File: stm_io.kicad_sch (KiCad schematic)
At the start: 0 parts

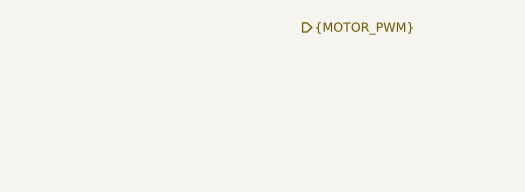
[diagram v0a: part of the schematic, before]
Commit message: schematic: continue project architecture
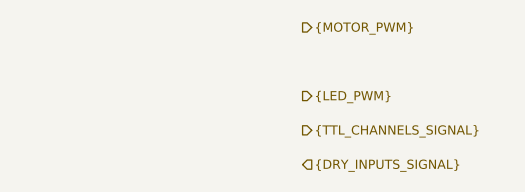
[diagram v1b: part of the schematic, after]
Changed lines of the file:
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@@
 	(generator_version "9.0")
 	(paper "A4")
+	(hierarchical_label "{DRY_INPUTS_SIGNAL}"
+		(shape input)
+		(at 181.61 66.04 0)
+		(effects
+			(font
+				(size 1.016 1.016)
+			)
+			(justify left)
+		)
+	)
 	(hierarchical_label "{MOTOR_PWM}"
 		(shape output)
@@
 		)
 	)
+	(hierarchical_label "{LED_PWM}"
+		(shape output)
+		(at 181.61 58.42 0)
+		(effects
+			(font
+				(size 1.016 1.016)
+			)
+			(justify left)
+		)
+	)
 	(hierarchical_label "H_BEAT"
 		(shape input)
@@
 		)
 	)
+	(hierarchical_label "{TTL_CHANNELS_SIGNAL}"
+		(shape output)
+		(at 181.61 62.23 0)
+		(effects
+			(font
+				(size 1.016 1.016)
+			)
+			(justify left)
+		)
+	)

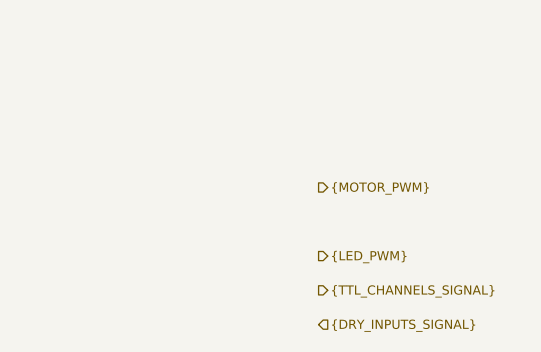
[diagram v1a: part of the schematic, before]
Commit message: schematic: add project structure wiring
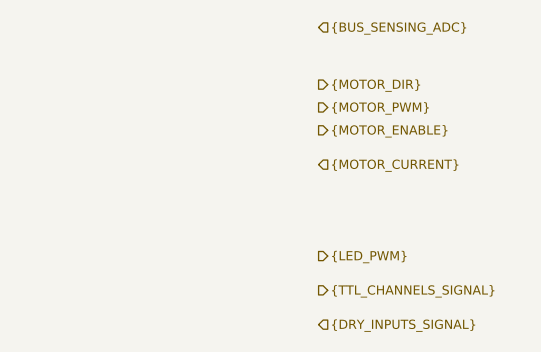
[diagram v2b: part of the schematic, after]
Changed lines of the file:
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@@
 		)
 	)
-	(hierarchical_label "{MOTOR_PWM}"
+	(hierarchical_label "{MOTOR_ENABLE}"
 		(shape output)
-		(at 181.61 50.8 0)
+		(at 181.61 44.45 0)
+		(effects
+			(font
+				(size 1.016 1.016)
+			)
+			(justify left)
+		)
+	)
+	(hierarchical_label "{MOTOR_DIR}"
+		(shape output)
+		(at 181.61 39.37 0)
 		(effects
 			(font
@@
 			)
 			(justify right)
+		)
+	)
+	(hierarchical_label "{BUS_SENSING_ADC}"
+		(shape input)
+		(at 181.61 33.02 0)
+		(effects
+			(font
+				(size 1.016 1.016)
+			)
+			(justify left)
 		)
 	)
@@
 		)
 	)
+	(hierarchical_label "{MOTOR_PWM}"
+		(shape output)
+		(at 181.61 41.91 0)
+		(effects
+			(font
+				(size 1.016 1.016)
+			)
+			(justify left)
+		)
+	)
 	(hierarchical_label "{UART}"
 		(shape bidirectional)
@@
 		)
 	)
+	(hierarchical_label "{MOTOR_CURRENT}"
+		(shape input)
+		(at 181.61 48.26 0)
+		(effects
+			(font
+				(size 1.016 1.016)
+			)
+			(justify left)
+		)
+	)

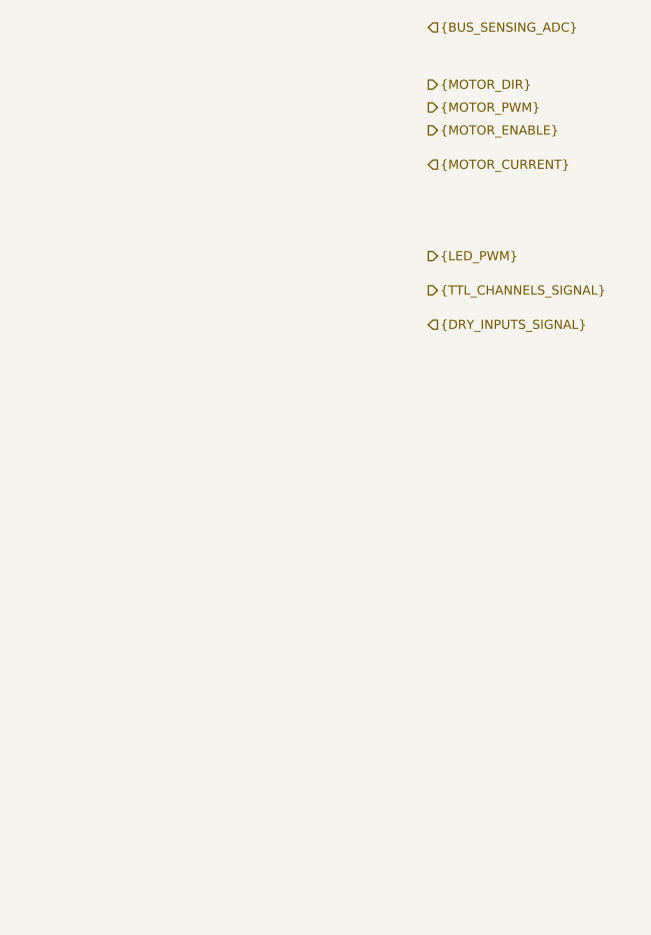
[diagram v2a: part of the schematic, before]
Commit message: Add power stages
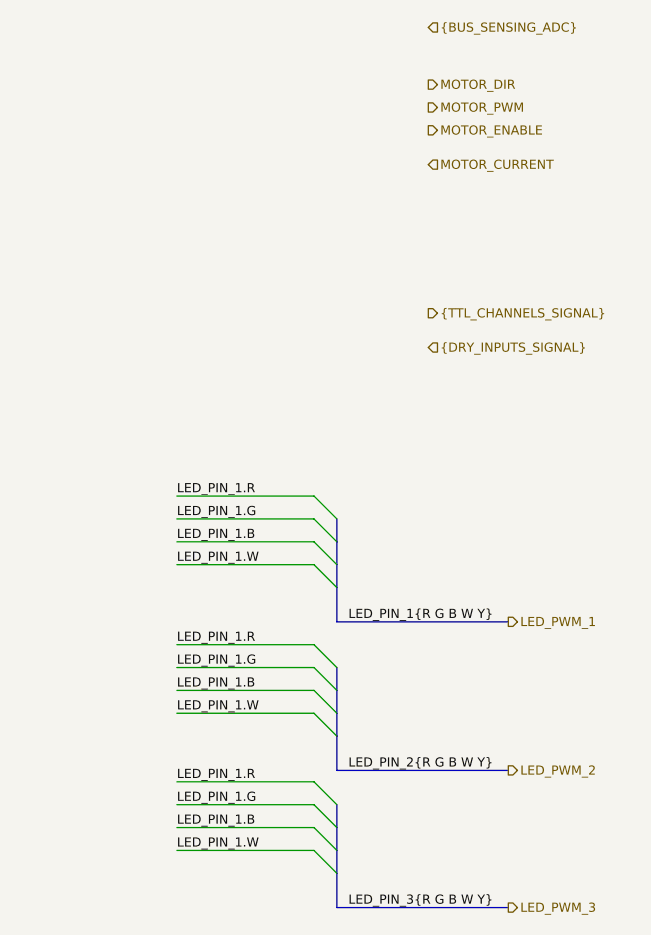
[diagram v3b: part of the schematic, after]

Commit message: Add power supplies
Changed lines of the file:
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@@
+		)
+	)
+	(hierarchical_label "LED_CURRENT"
+		(shape input)
+		(at 191.77 148.59 180)
+		(effects
+			(font
+				(size 1.016 1.016)
+			)
+			(justify right)
 		)
 	)
@@
 			)
 			(justify left)
+		)
+	)
+	(hierarchical_label "~{FAULT}"
+		(shape input)
+		(at 191.77 142.24 180)
+		(effects
+			(font
+				(size 1.016 1.016)
+			)
+			(justify right)
 		)
 	)
@@
 		)
 	)
-	(hierarchical_label "{BUS_SENSING_ADC}"
+	(hierarchical_label "BUS_SENSING_ADC"
 		(shape input)
 		(at 181.61 33.02 0)
@@
 			)
 			(justify left)
+		)
+	)
+	(hierarchical_label "~{FAULT_RESET}"
+		(shape output)
+		(at 191.77 144.78 180)
+		(effects
+			(font
+				(size 1.016 1.016)
+			)
+			(justify right)
 		)
 	)
@@
 		)
 	)
+	(hierarchical_label "CURRENT_LIMIT_SET"
+		(shape output)
+		(at 191.77 139.7 180)
+		(effects
+			(font
+				(size 1.016 1.016)
+			)
+			(justify right)
+		)
+	)

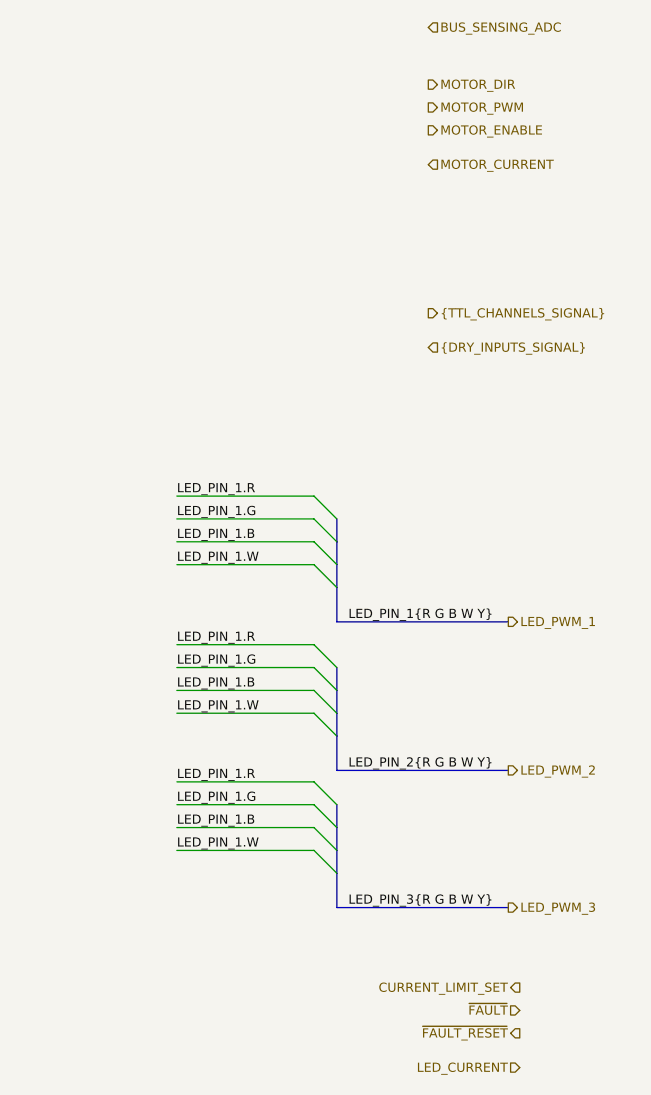
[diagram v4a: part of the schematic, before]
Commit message: Remove STM
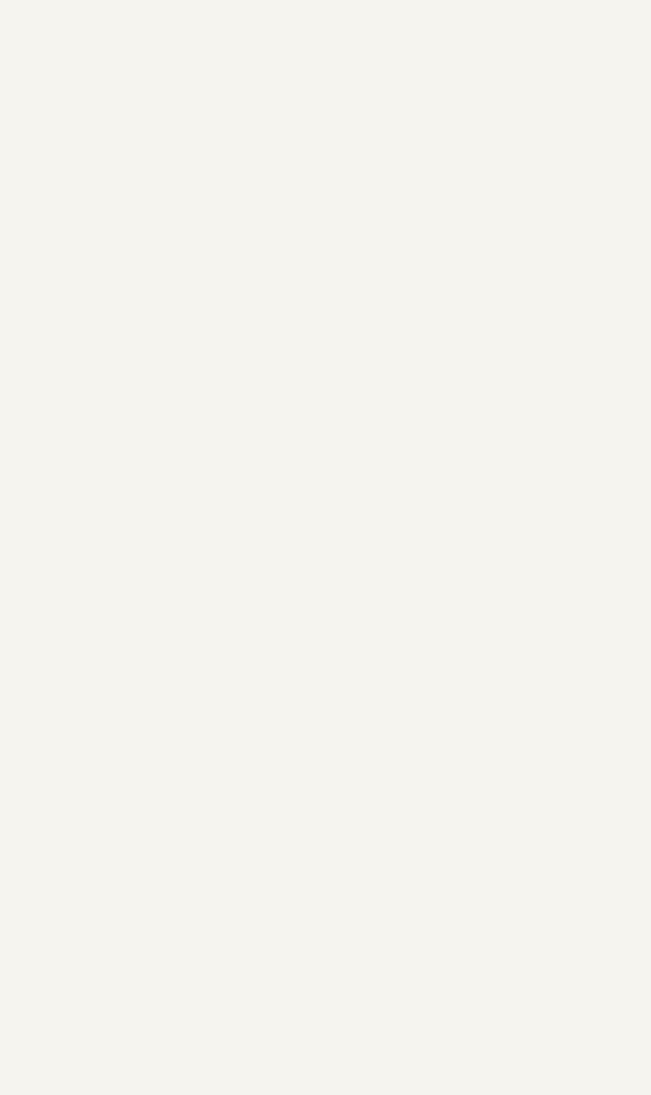
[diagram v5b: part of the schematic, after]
